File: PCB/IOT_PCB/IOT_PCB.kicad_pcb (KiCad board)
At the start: 2 copper layers, 50 x 72 mm, 35 parts, among them J1 Screw_Terminal, J2 Screw_Terminal, J3 USB-C Conn, U1 ESP32-S3-MINI-1, U2 BME280, U3 SCD41-D-R2, U4 ENS160-BGLM, U5 3V3 Reg, U6 1V8 Reg, U7 ESD Suppresion

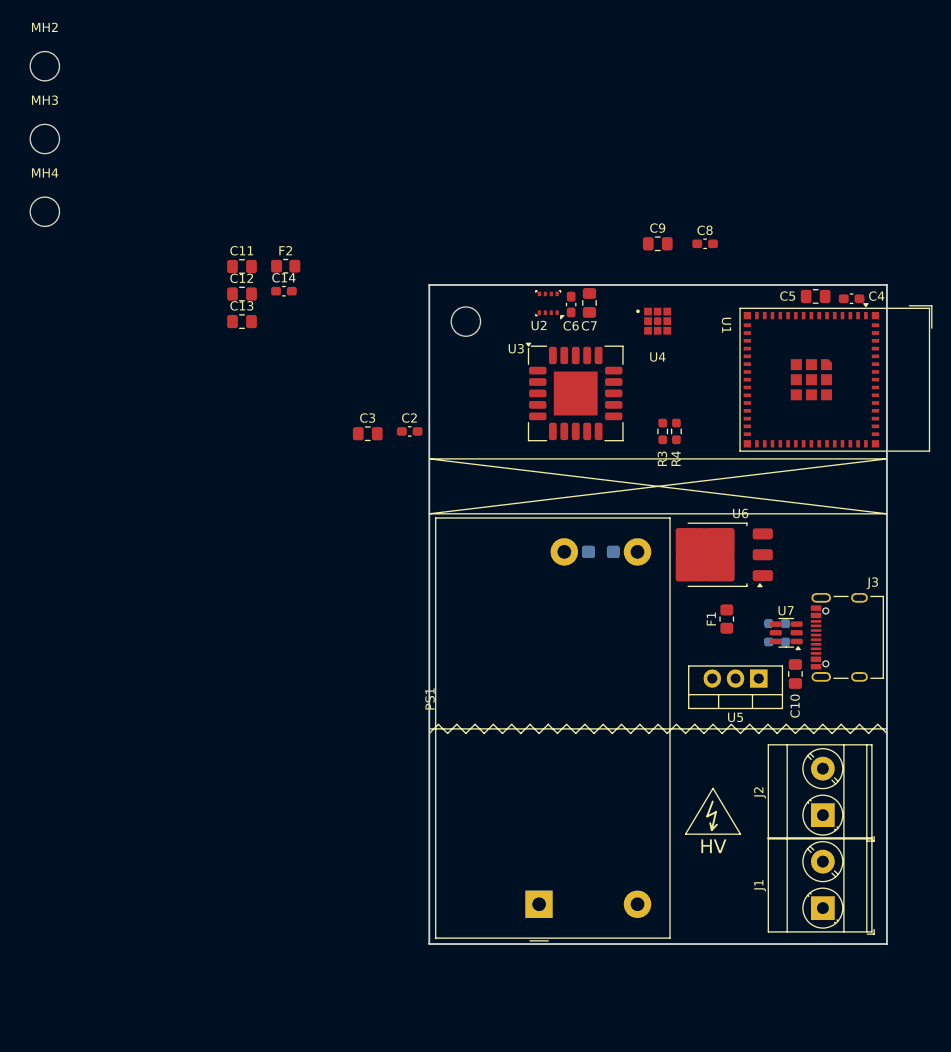
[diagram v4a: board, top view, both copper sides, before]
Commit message: Changed Power Supply
Power supply changed from Mean Well to RECOM
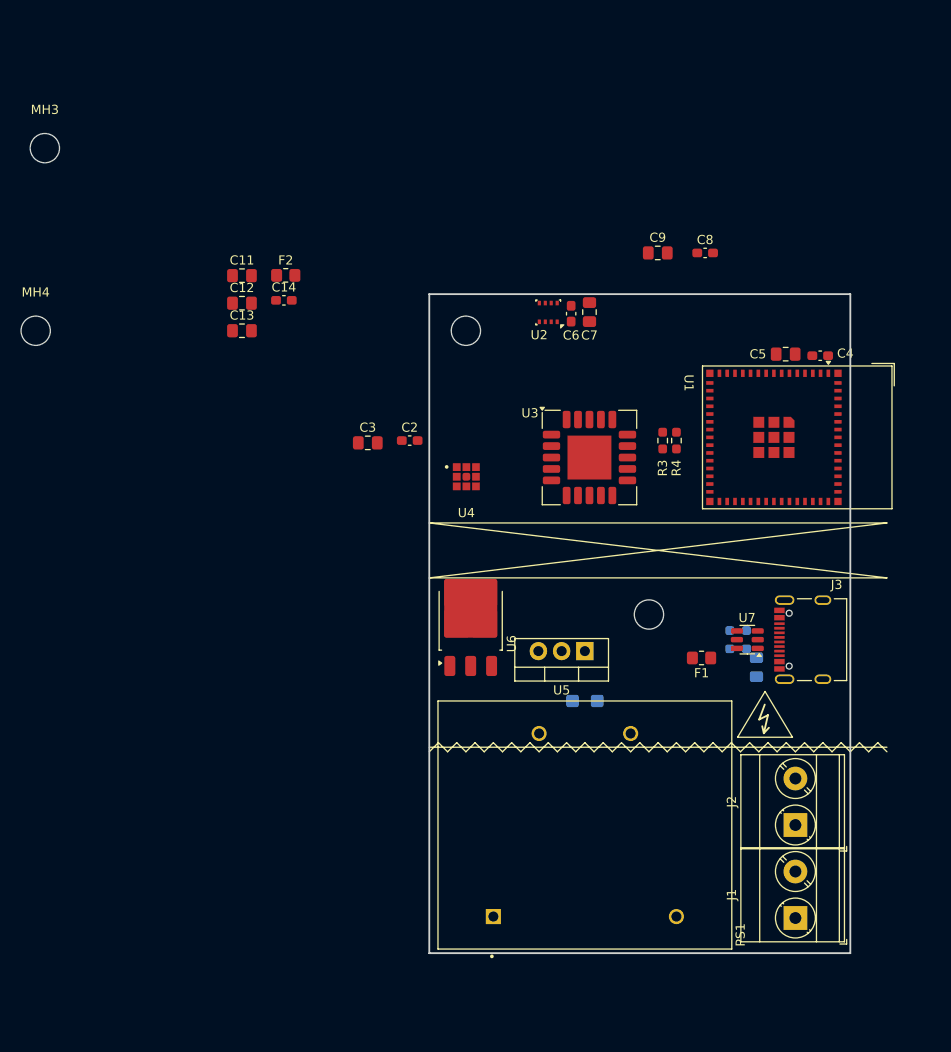
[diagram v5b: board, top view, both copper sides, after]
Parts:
- C10: moved to B.Cu
- PS1: value IRM-05-5 -> RAC05E-05SKT; footprint Converter_ACDC:Converter_ACDC_MeanWell_IRM-05-xx_THT -> RAC05E_05SKT:CONV_RAC05E-05SKT
- moved MH2 89.1 mm to (144.0, 115.0)
- moved U6 27.8 mm to (124.5, 115.6), turned to 90 degrees
- moved U4 26.9 mm to (124.0, 100.0)
- moved U5 19.2 mm to (137.0, 119.0)
- moved C1 16.4 mm to (137.0, 124.5), turned to 180 degrees
- moved MH4 13.0 mm to (77.0, 84.0)
- moved PS1 10.00 mm to (137.0, 138.0)
- moved U1 7.52 mm to (160.2, 95.7)
- moved U3 7.16 mm to (137.5, 97.8)
- moved C4 7.11 mm to (162.7, 86.7)
- moved C5 7.11 mm to (158.9, 86.6)
- moved F1 5.06 mm to (149.7, 119.8), turned to 180 degrees
- moved C10 4.32 mm to (155.7, 120.8)
- moved R1 4.32 mm to (153.7, 118.8)
- moved R2 4.32 mm to (153.7, 116.8)
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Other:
- board size 50 x 72 mm -> 46 x 72 mm
- board text removed: "HV"

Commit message: Finalized Design (Rev A)
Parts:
- removed MH3, MH4: MountingHole, MountingHole:MountingHole_3.2mm_M3
- added C15: 10µF, Capacitor_SMD:C_0805_2012Metric_Pad1.18x1.45mm_HandSolder, F.Cu at (141.4, 87.9)
- added D1: ~, Diode_SMD:D_0805_2012Metric_Pad1.15x1.40mm_HandSolder, F.Cu at (156.0, 123.2)
- added D2: ~, Diode_SMD:D_0805_2012Metric_Pad1.15x1.40mm_HandSolder, F.Cu at (144.6, 120.1)
- added J4: SM06B-GHS-TB, Connector_JST:JST_GH_SM06B-GHS-TB_1x06-1MP_P1.25mm_Horizontal, F.Cu at (154.7, 83.3)
- added J6: Screw_Terminal_01x04, TerminalBlock_MetzConnect:TerminalBlock_MetzConnect_Type101_RT01604HBWC_1x04_P5.08mm_Horizontal, F.Cu at (124.4, 113.4)
- added R5: 4.7kΩ, Resistor_SMD:R_0603_1608Metric_Pad0.98x0.95mm_HandSolder, F.Cu at (159.9, 89.5)
- added R6: 4.7kΩ, Resistor_SMD:R_0603_1608Metric_Pad0.98x0.95mm_HandSolder, F.Cu at (162.5, 91.0)
- added REF**: SEN54, Library_Theo:SEN54, F.Cu at (120.0, 80.0)
- added TP1: ~, Connector_Pin:Pin_D1.0mm_L10.0mm, F.Cu at (141.8, 94.3)
- added TP2: ~, Connector_Pin:Pin_D1.0mm_L10.0mm, F.Cu at (141.8, 99.0)
- added TP3: ~, Connector_Pin:Pin_D1.0mm_L10.0mm, F.Cu at (157.1, 118.9)
- added TP5: ~, Connector_Pin:Pin_D1.0mm_L10.0mm, F.Cu at (145.5, 117.5)
- added TP6: ~, Connector_Pin:Pin_D1.0mm_L10.0mm, F.Cu at (148.7, 117.7)
- C1: moved to F.Cu
- U1: footprint RF_Module:ESP32-S2-MINI-1 -> PCM_Espressif:ESP32-S3-MINI-1
- U5: footprint Package_TO_SOT_THT:TO-220-3_Vertical -> Package_TO_SOT_SMD:TO-252-3_TabPin2
- U6: footprint Package_TO_SOT_SMD:TO-252-3_TabPin2 -> Package_TO_SOT_SMD:SOT-223-3_TabPin2
- moved F2 72.4 mm to (155.5, 129.2), turned to 90 degrees
- moved C12 70.5 mm to (153.6, 126.2)
- moved C11 69.5 mm to (152.7, 122.8), turned to -90 degrees
- moved C13 54.6 mm to (140.3, 120.3)
- moved C3 47.6 mm to (160.8, 93.1)
- moved C2 42.8 mm to (160.6, 94.9)
- moved C14 42.0 mm to (134.7, 109.5), turned to 180 degrees
- moved J1 34.5 mm to (125.7, 151.9), turned to -90 degrees
- moved J2 34.4 mm to (125.7, 140.4), turned to -90 degrees
- moved U2 30.5 mm to (163.5, 82.2), turned to 0 degrees
- moved C6 27.3 mm to (162.5, 86.4)
- moved C7 27.2 mm to (164.3, 86.5)
- moved U4 22.8 mm to (139.8, 83.3)
- moved C1 16.8 mm to (152.9, 129.8), turned to 90 degrees
- moved U3 16.4 mm to (153.2, 93.2), turned to 90 degrees
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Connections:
- F1 pad 2: Net-(D2-A) -> /Fuse_VBUS
- F2 pad 2: Net-(D1-A) -> /Fuse_VSUPPLY
- J1 pad 1: AC_L -> AC_N
- J1 pad 2: AC_L -> AC_N
- J2 pad 1: AC_N -> AC_L
- J2 pad 2: AC_N -> AC_L
- J3 pad SH1: unconnected-(J3-SHIELD-PadSH1) -> GND
- J3 pad SH2: unconnected-(J3-SHIELD-PadSH2) -> GND
- J3 pad SH3: unconnected-(J3-SHIELD-PadSH3) -> GND
- J3 pad SH4: unconnected-(J3-SHIELD-PadSH4) -> GND
- U2 pad 8: unconnected-(U2-VDD-Pad8) -> +3V3
- U3 pad 1: (no net) -> unconnected-(U3-Pad1)
- U3 pad 11: (no net) -> unconnected-(U3-Pad11)
- U3 pad 12: (no net) -> unconnected-(U3-Pad12)
- U3 pad 13: (no net) -> unconnected-(U3-Pad13)
- U3 pad 14: (no net) -> unconnected-(U3-Pad14)
- U3 pad 15: (no net) -> unconnected-(U3-Pad15)
- U3 pad 16: (no net) -> unconnected-(U3-Pad16)
- U3 pad 17: (no net) -> unconnected-(U3-Pad17)
- U3 pad 18: (no net) -> unconnected-(U3-Pad18)
- U3 pad 2: (no net) -> unconnected-(U3-Pad2)
- U3 pad 3: (no net) -> unconnected-(U3-Pad3)
- U3 pad 4: (no net) -> unconnected-(U3-Pad4)
- U3 pad 5: (no net) -> unconnected-(U3-Pad5)
- U3 pad 8: (no net) -> unconnected-(U3-Pad8)
- U4 pad 4: unconnected-(U4-VDD-Pad4) -> +1V8
- U4 pad 7: unconnected-(U4-~{CS}-Pad7) -> +3V3
- U4 pad 8: unconnected-(U4-VSS-Pad8) -> GND
- U4 pad 9: unconnected-(U4-VSS__1-Pad9) -> GND
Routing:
- net +3V3: track 0.00 -> 154.0 mm, vias 0 -> 9
- net +5V: track 0.00 -> 96.3 mm, vias 0 -> 2
- net /SCL: track 0.00 -> 93.6 mm, vias 0 -> 4
- net /SDA: track 0.00 -> 72.7 mm, vias 0 -> 1
- net +1V8: track 0.00 -> 49.4 mm
- net AC_L: track 0.00 -> 38.5 mm
- net VBUS: track 0.00 -> 34.1 mm, vias 0 -> 2
- net Net-(R3-Pad1): track 0.00 -> 24.7 mm, vias 0 -> 1
- net Net-(R4-Pad1): track 0.00 -> 18.1 mm, vias 0 -> 1
- net Net-(J3-DN1): track 0.00 -> 16.6 mm
- net Net-(J3-DP1): track 0.00 -> 15.5 mm
- net Net-(J3-CC1): track 0.00 -> 13.5 mm, vias 0 -> 1
- net Net-(J3-CC2): track 0.00 -> 13.1 mm, vias 0 -> 1
- net GND: track 0.00 -> 9.34 mm, vias 0 -> 52
- net /Fuse_VSUPPLY: track 0.00 -> 4.24 mm
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- added copper zone on F.Cu, net +3V3
- added copper zone on B.Cu, net AC_L
- added copper zone on F.Cu, net AC_L
- added copper zone on B.Cu, net AC_N
- added copper zone on F.Cu, net AC_N
- added copper zone on B.Cu, net GND
- added copper zone on F.Cu, net GND
- added copper zone on F.Cu, net VSUPPLY
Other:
- board size 46 x 72 mm -> 46 x 80 mm
- board text added: "1V8"
- board text added: "3V3"
- board text added: "5V0"
- board text added: "GND"
- board text added: "L"
- board text added: "N"
